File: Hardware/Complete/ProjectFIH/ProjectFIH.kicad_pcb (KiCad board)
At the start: 2 copper layers, 84 parts, among them J1 Conn_01x02_Male, J10 Payload LED, J2 Power, J3 Power LED, J4 MCU Fail LED, J5 Heater LED, J6 Heater, J7 UART, J8 AVR-ISP-10, J9 Payload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

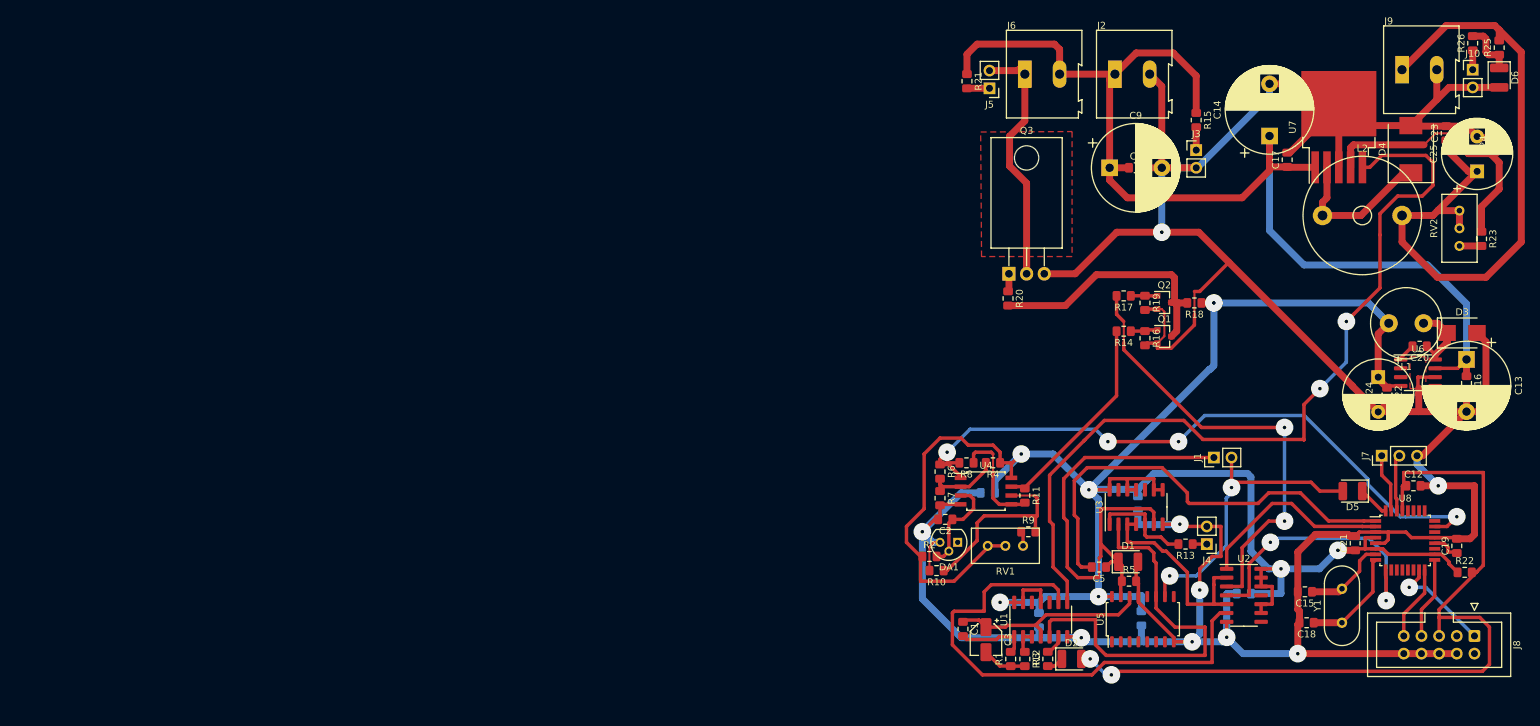
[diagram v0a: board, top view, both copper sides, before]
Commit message: Small corrections after laying IRL parts out
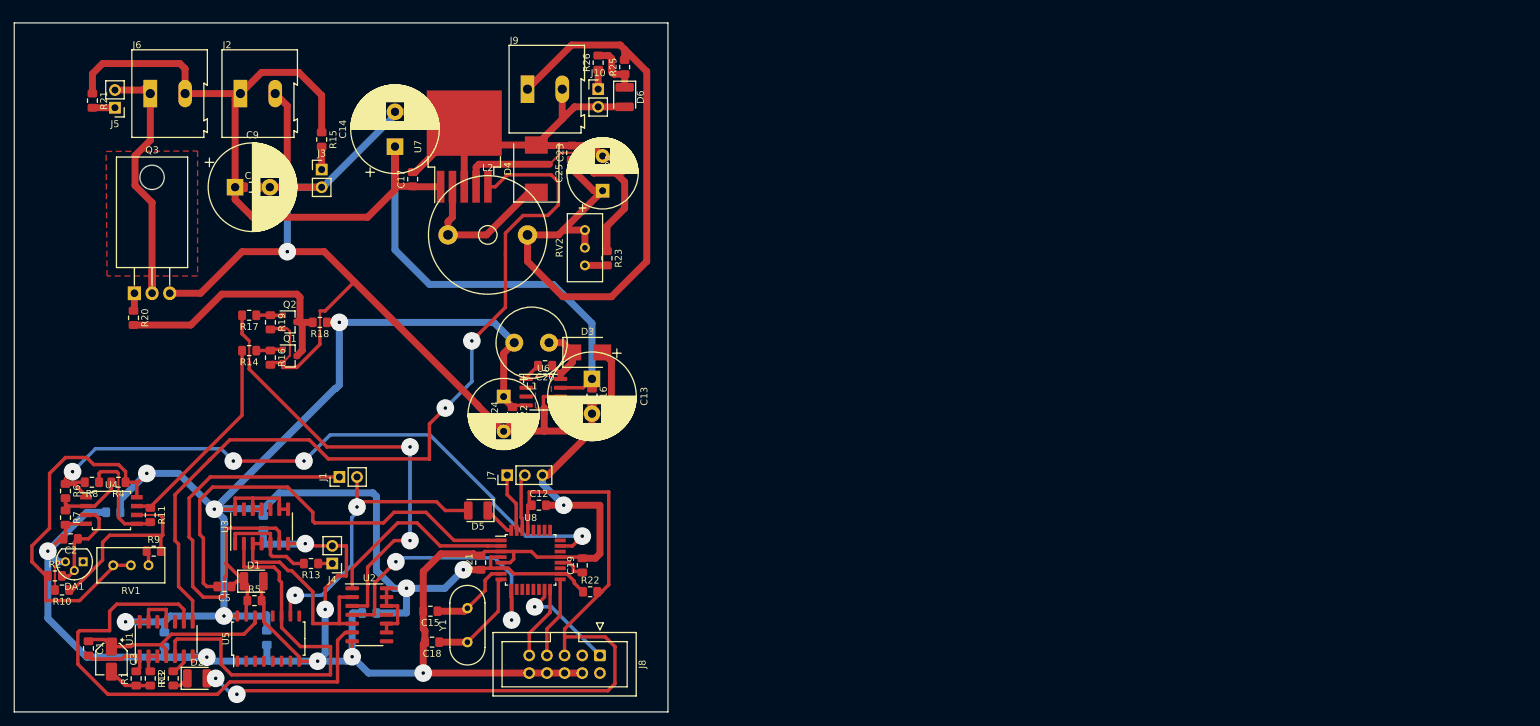
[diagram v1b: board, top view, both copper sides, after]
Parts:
- C13, C14, C9: footprint Capacitor_THT:CP_Radial_D12.5mm_P7.50mm -> Capacitor_THT:CP_Radial_D12.5mm_P5.00mm
- moved C8 127.3 mm to (46.7, 36.3)
- moved C1 125.8 mm to (23.4, 102.6)
- moved C4 125.8 mm to (34.3, 101.4)
- moved C6 125.8 mm to (26.9, 83.1)
- moved D2 125.8 mm to (39.0, 106.9)
- moved D6 125.8 mm to (100.5, 23.4)
- moved DA1 125.8 mm to (22.6, 90.2)
- moved J9 125.8 mm to (86.5, 22.2)
- moved L1 125.8 mm to (89.6, 58.7)
- moved Q2 125.8 mm to (52.3, 55.7)
- moved R25 125.8 mm to (100.5, 19.1)
- moved R4 125.8 mm to (27.7, 78.7)
- moved U2 125.8 mm to (63.8, 97.8)
- moved U3 125.8 mm to (48.3, 85.1)
- moved U5 125.8 mm to (49.2, 101.2)
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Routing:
- net GND: track 524.6 -> 527.1 mm
- net +24V: track 169.9 -> 171.1 mm
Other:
- board outline added: 94 x 99.1 mm

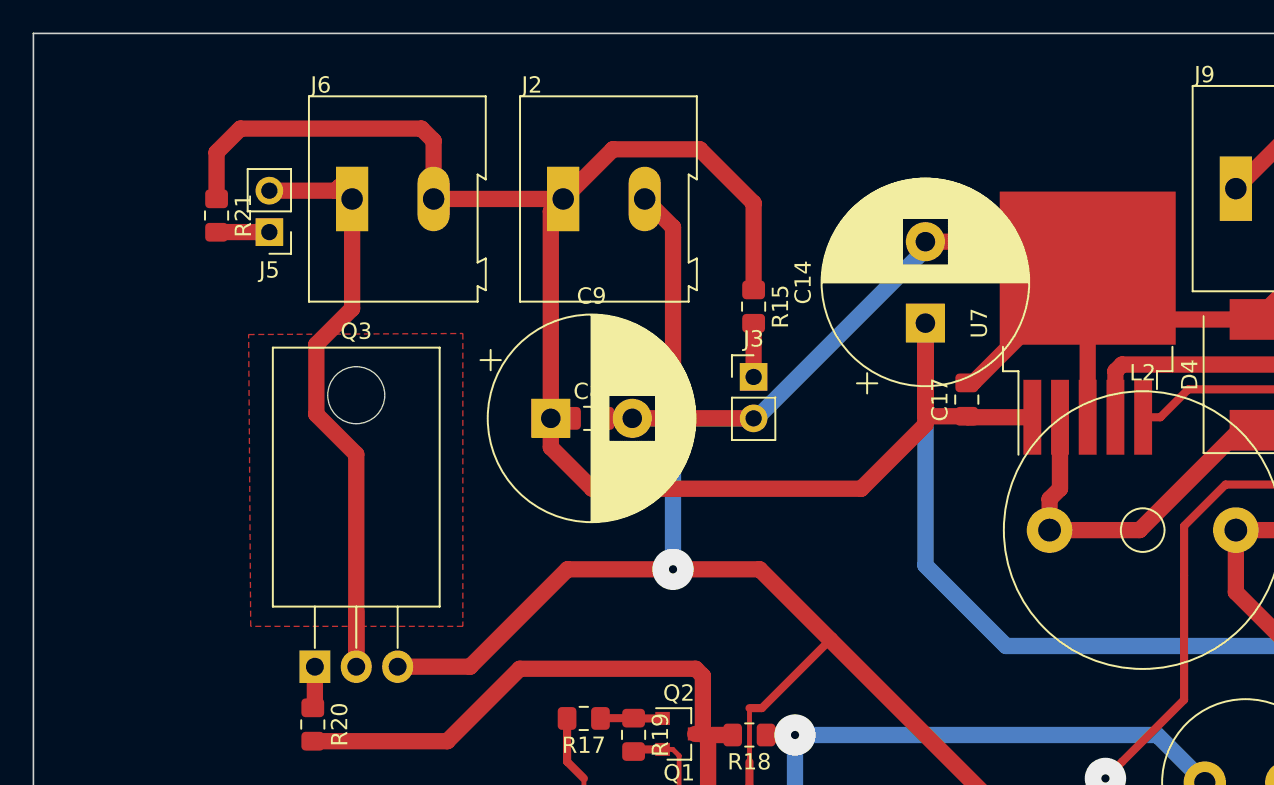
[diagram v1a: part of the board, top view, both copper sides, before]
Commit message: Started tracks widening and filling
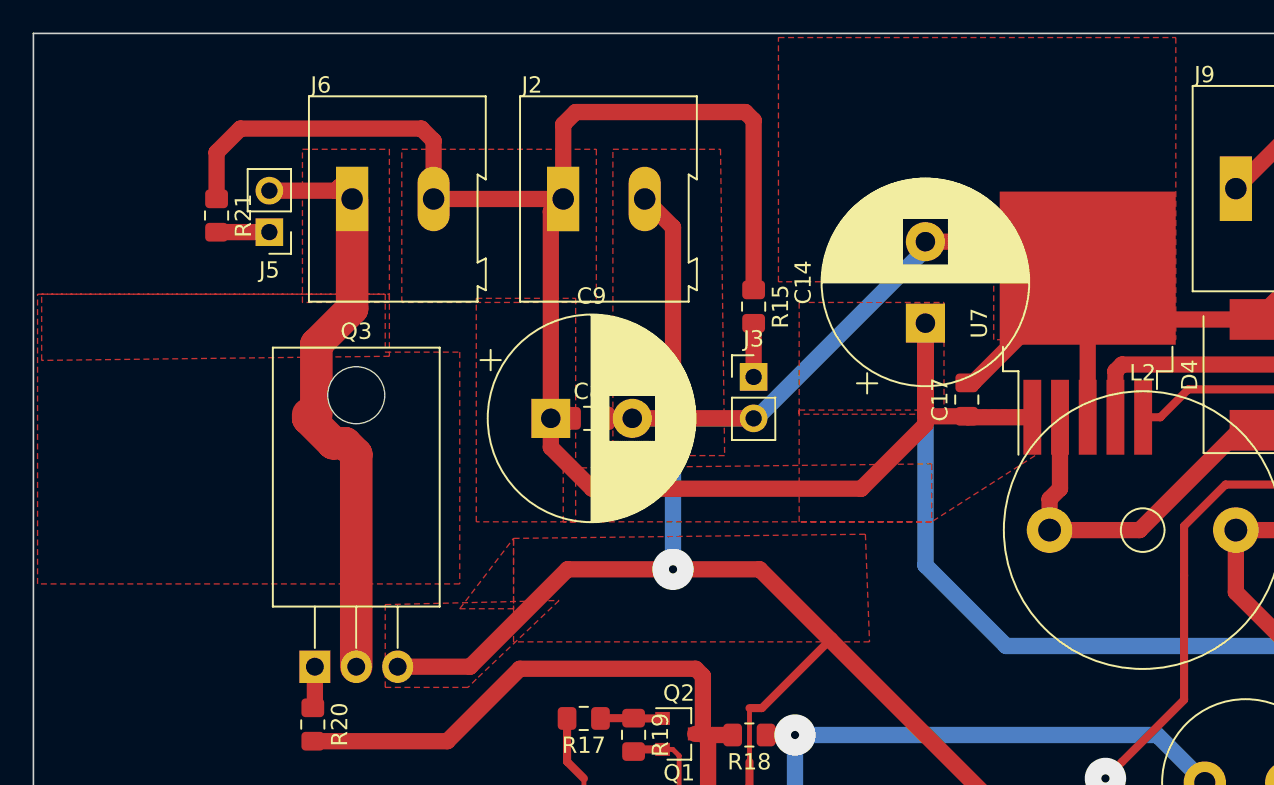
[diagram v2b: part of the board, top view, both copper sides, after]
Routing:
- net +24V: track 171.1 -> 178.7 mm
- net Net-(J5-Pad2): track 41.0 -> 45.1 mm
- net GND: track 527.1 -> 528.7 mm
- added copper zone on F.Cu, net +24V

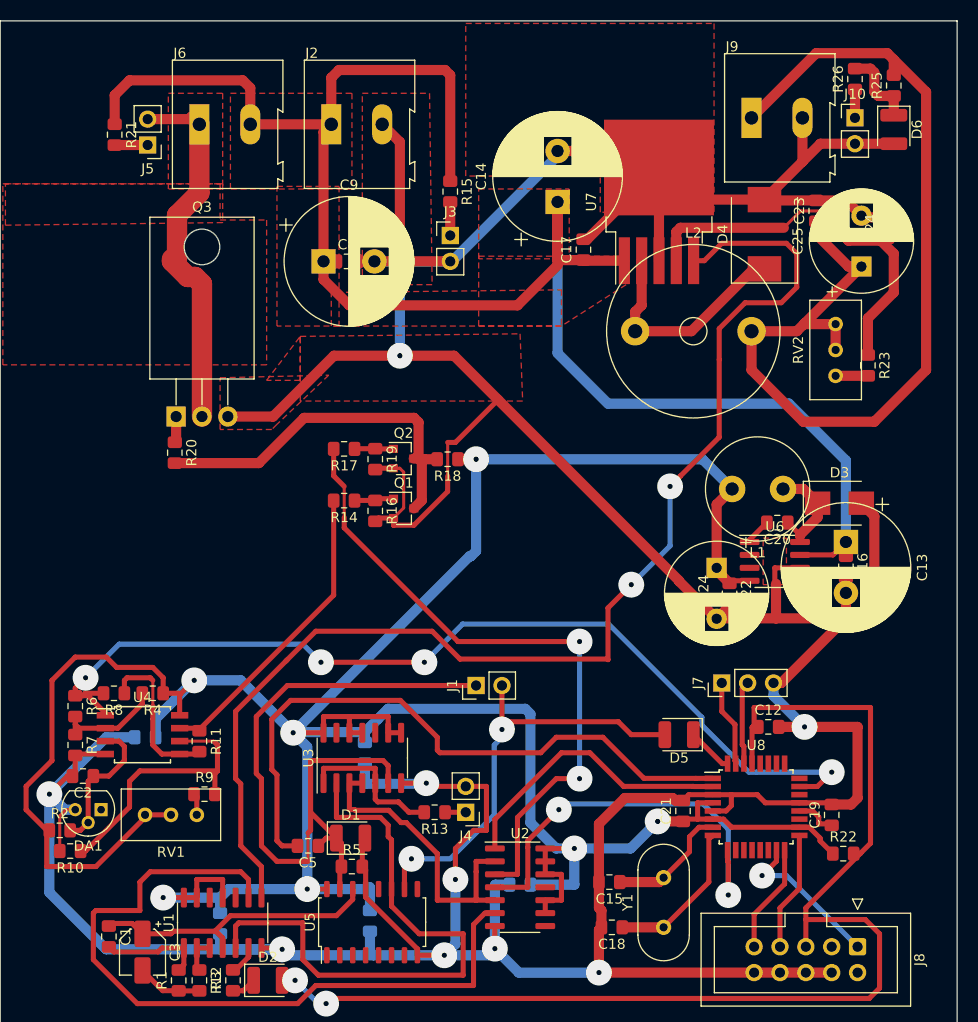
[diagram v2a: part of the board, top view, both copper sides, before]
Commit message: Flipped some (but not all needed) parts to other side
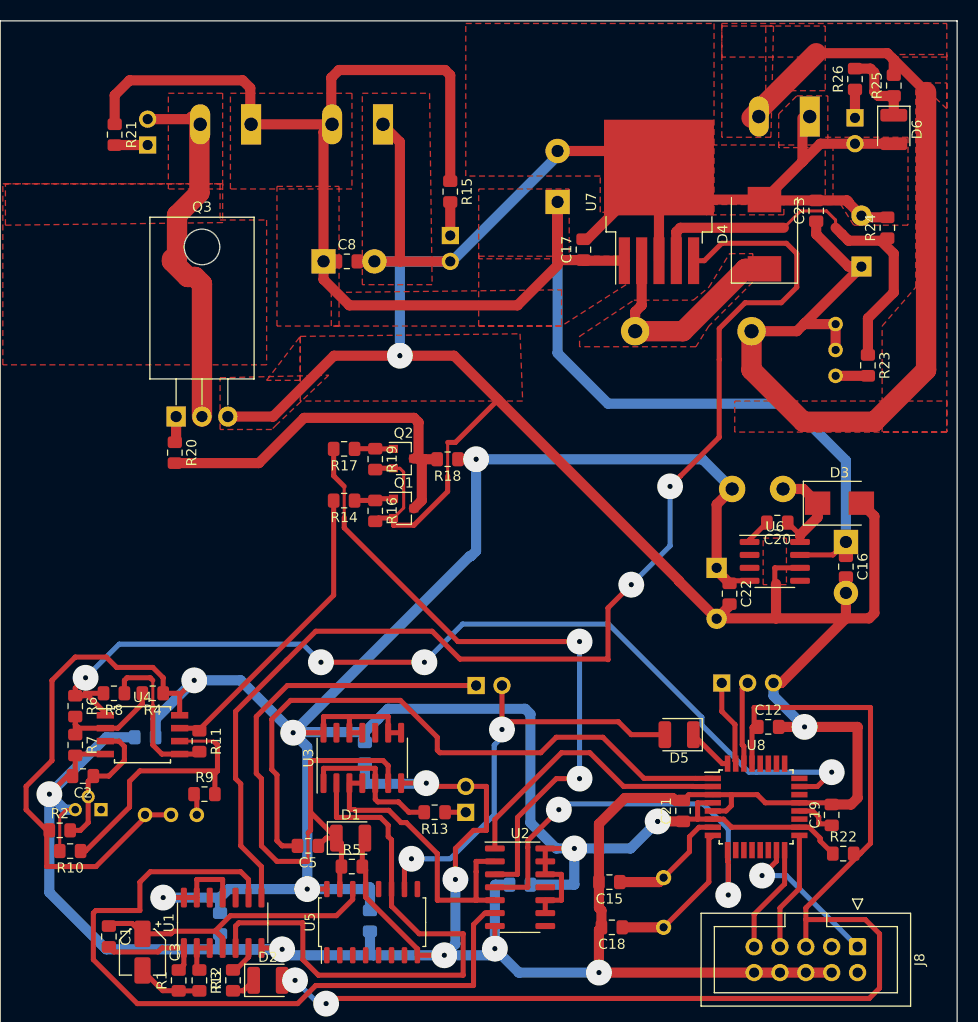
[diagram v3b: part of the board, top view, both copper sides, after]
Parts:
- C13, C14, C24, C25, C9, DA1, J1, J10, J2, J3, J4, J5, J6, J7, J9, L1, L2, RV1, RV2, Y1: moved to B.Cu
- moved J9 5.72 mm to (92.2, 22.1), turned to 180 degrees
- moved J2 5.08 mm to (50.3, 22.9), turned to 180 degrees
- moved J6 5.08 mm to (37.3, 22.9), turned to 180 degrees
- turned J1 to 270 degrees
- turned J10 to 180 degrees
- turned J3 to 180 degrees
- turned J4 to 0 degrees
- turned J5 to 0 degrees
- turned J7 to 270 degrees
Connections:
- J2 pad 1: +24V -> GND
- J2 pad 2: GND -> +24V
- J6 pad 1: Net-(J5-Pad2) -> +24V
- J6 pad 2: +24V -> Net-(J5-Pad2)
- J9 pad 1: Net-(C23-Pad1) -> GND
- J9 pad 2: GND -> Net-(C23-Pad1)
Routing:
- added copper zone on F.Cu, net Net-(C23-Pad1)
- added copper zone on F.Cu, net Net-(D4-Pad1)

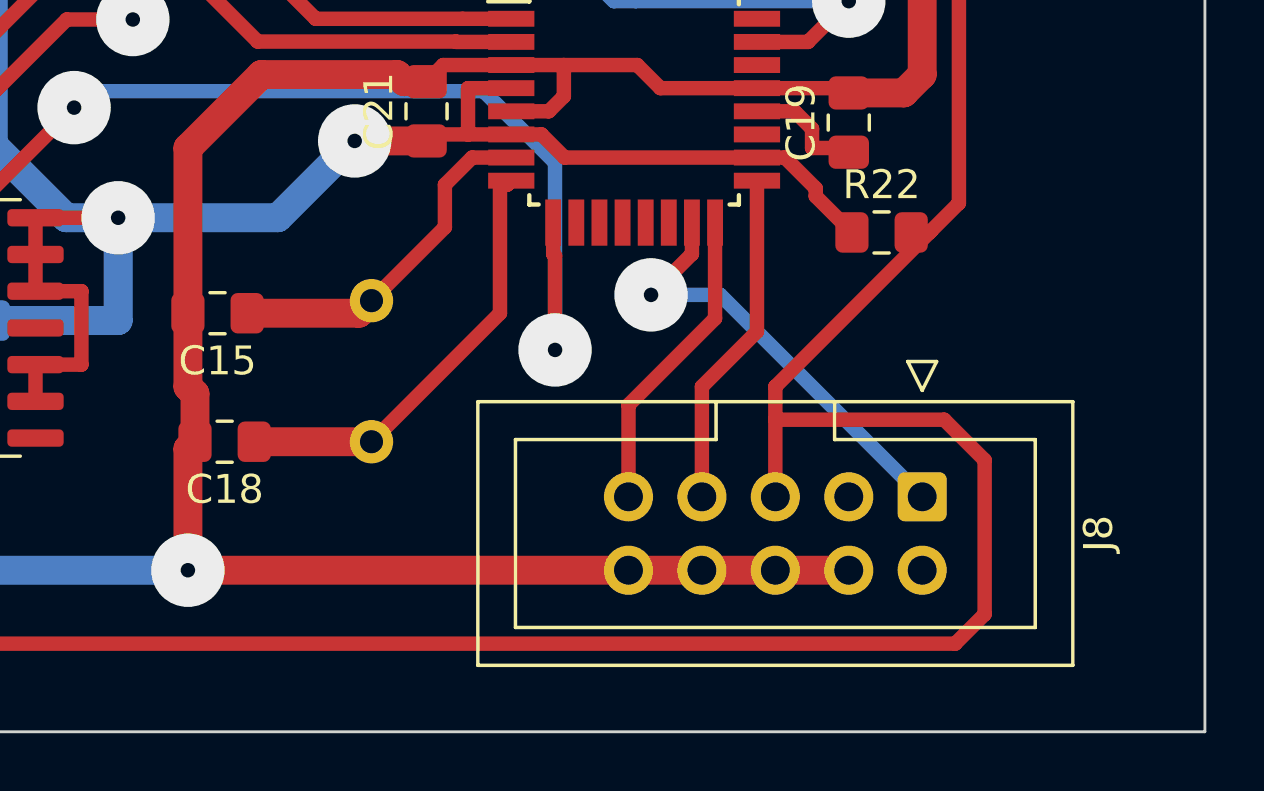
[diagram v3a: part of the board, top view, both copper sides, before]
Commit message: Everything is on correct sides
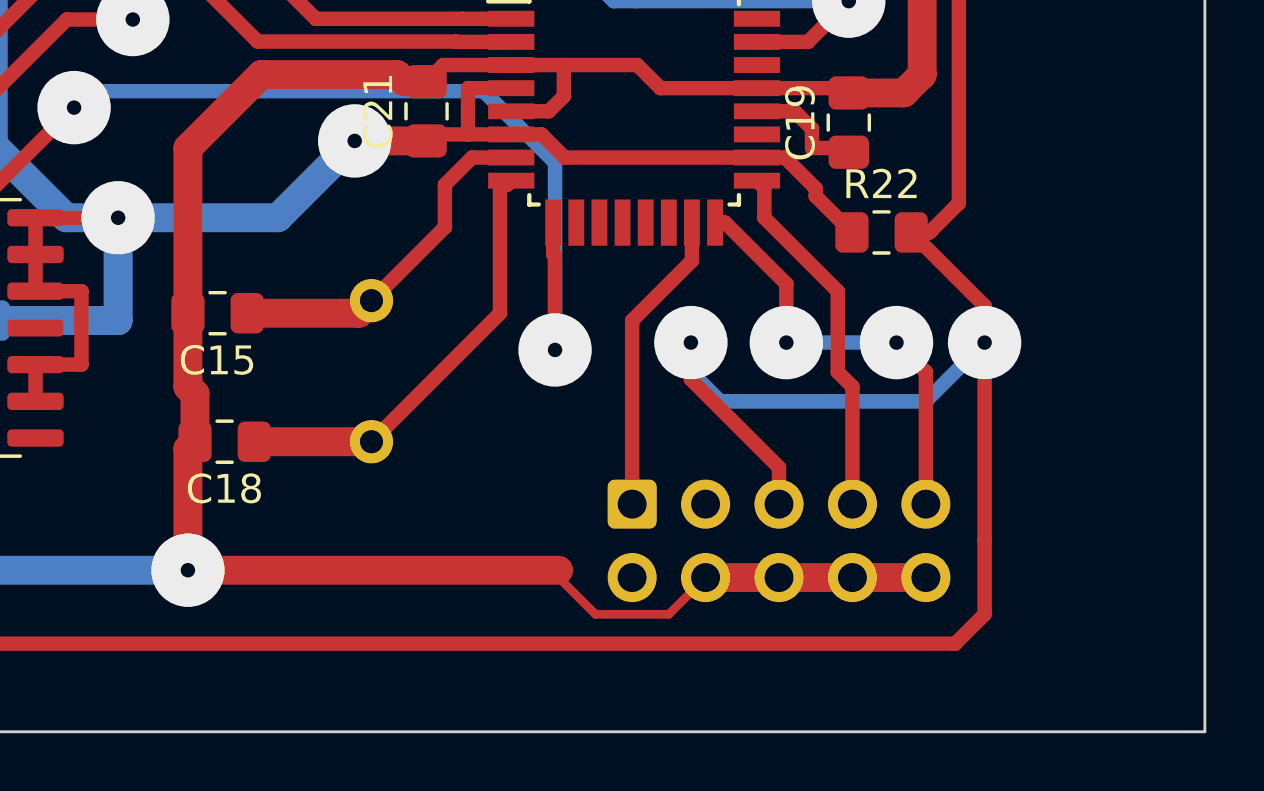
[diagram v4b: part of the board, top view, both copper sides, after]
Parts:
- J8: moved to B.Cu
- moved J8 10.0 mm to (86.9, 103.9)
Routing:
- net MCUReset: track 117.3 -> 126.2 mm, vias 2 -> 4
- net Net-(J8-Pad1): track 15.4 -> 10.6 mm, vias 1 -> 0
- net Net-(J8-Pad9): track 10.7 -> 15.2 mm, vias 0 -> 2
- net GND: track 528.7 -> 532.7 mm
- net Net-(J8-Pad7): track 11.7 -> 12.6 mm
